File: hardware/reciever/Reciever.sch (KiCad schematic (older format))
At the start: 13 parts, among them J1 UART, J2 BTN, J3 OLED, P1 TC2030-CTX, SW1 RESET, U1 DS18B20, U2 BL654, U3 SHT30-DIS-B, U4 Coin Battery

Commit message: Add another schematic, add capacitor and rework 3v3 on laird
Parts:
- removed C1: 100nF, Capacitor_SMD:C_0603_1608Metric, symbol Device:C
- removed R4: 4,7k, Resistor_SMD:R_1206_3216Metric, symbol Device:R
- removed U1: DS18B20, Package_TO_SOT_THT:TO-92_Inline, symbol Sensor_Temperature:DS18B20
- removed U3: SHT30-DIS-B, SHT30-DIS-B:DFN250X250X100-9N, symbol SHT30-DIS-B:SHT30-DIS-B
- removed U4: Coin Battery, BS-3:BS3, symbol BS-3:BS-3
- added C? (x2): 100n, Capacitor_SMD:C_0805_2012Metric, symbol Device:C_Small
- added C? (x2): 10uF, symbol Device:CP_Small
- added C?: 22uF, symbol Device:CP_Small
- added D?: 1N5819HW-7-F, Diode_SMD:D_SOD-123, symbol Device:D_Schottky
- added J?: HEATER_CON, TerminalBlock_TE-Connectivity:TerminalBlock_TE_282834-2_1x02_P2.54mm_Horizontal, symbol Connector:Conn_01x02_Female
- added J?: PWR-9V, symbol Connector:Conn_01x02_Female
- added K?: RM50-xx21, Relay_THT:Relay_SPST_Finder_32.21-x300, symbol Relay:RM50-xx21
- added U?: DDC114EU, Package_TO_SOT_SMD:SOT-363_SC-70-6, symbol DDC114EU:DDC114EU
- added U?: AMS1117-3.3, Package_TO_SOT_SMD:SOT-223-3_TabPin2, symbol Regulator_Linear:AMS1117-3.3
- R1, R2: symbol Device:R -> Device:R_Small
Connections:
- net labels added: HEATER_PIN
- net labels removed: DS18B20
- wire segments 107 -> 128
- no-connect marks 44 -> 43
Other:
- moved on the sheet: J3

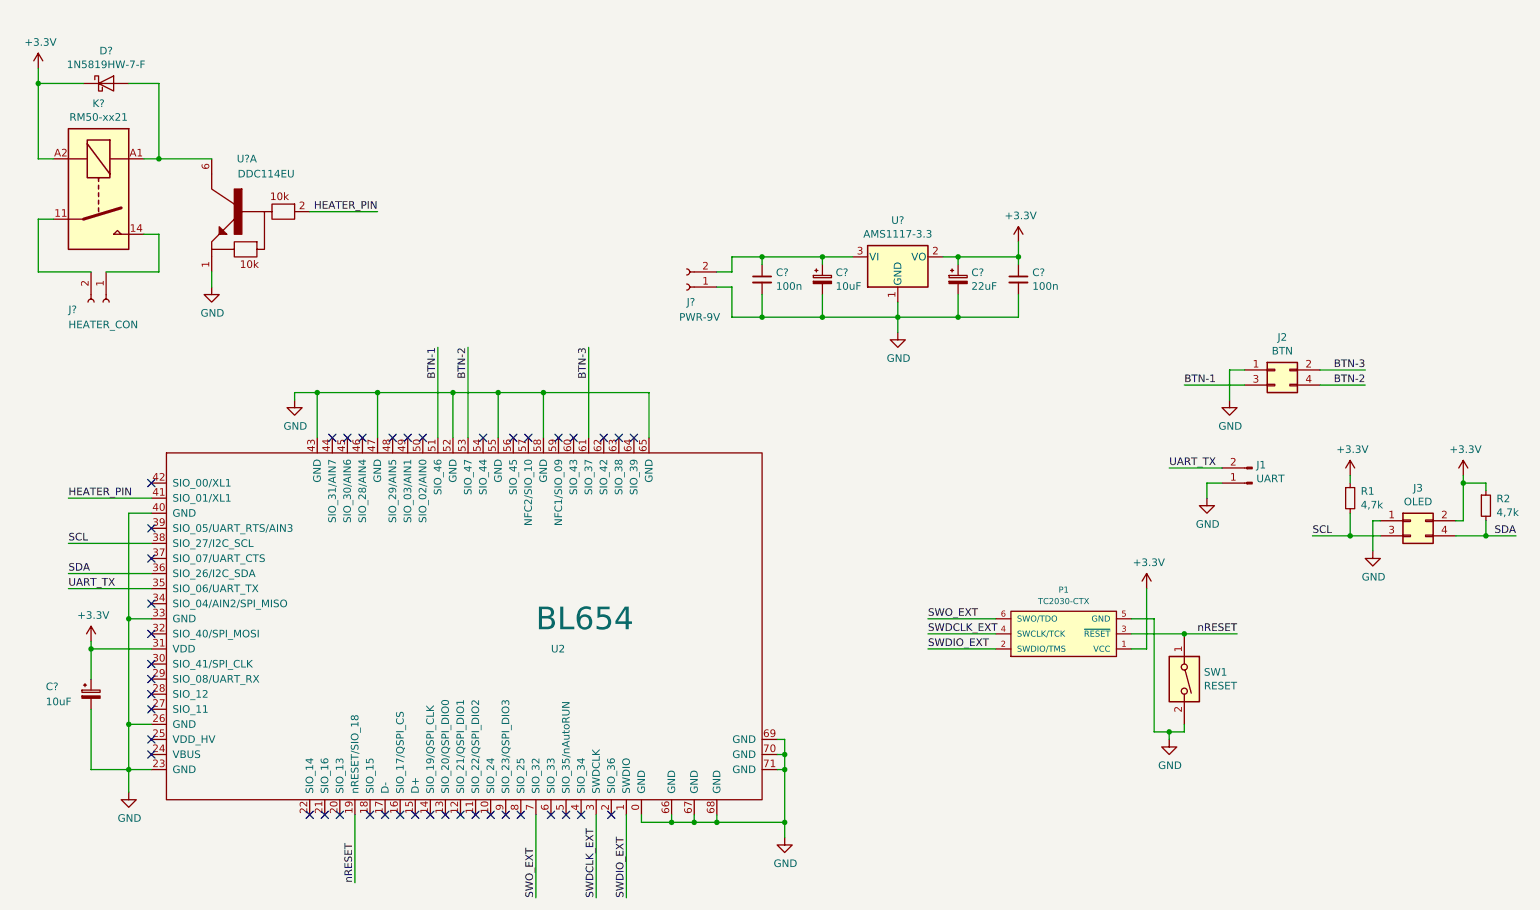
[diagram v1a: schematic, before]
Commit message: PCB layout fo reciever
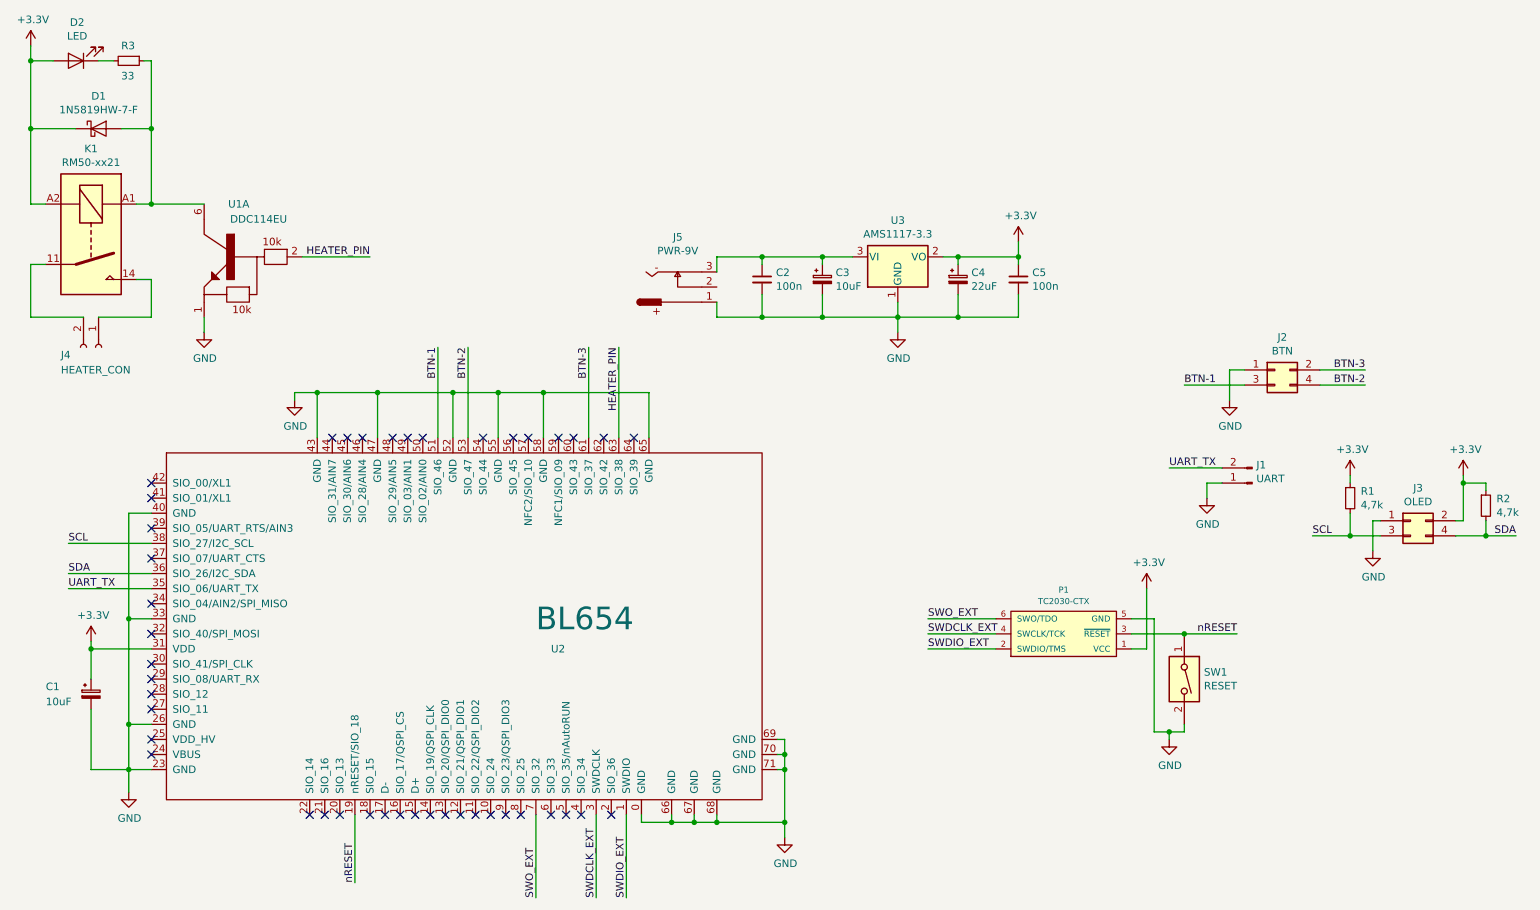
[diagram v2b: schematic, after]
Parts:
- removed J?: PWR-9V, symbol Connector:Conn_01x02_Female
- added D2: LED, Connector_PinHeader_2.54mm:PinHeader_1x02_P2.54mm_Vertical, symbol Device:LED
- added J5: PWR-9V, LUMBERG:1613-18, symbol Lumberg:1613-18
- added R3: 33, Resistor_SMD:R_1206_3216Metric, symbol Device:R_Small
- C1, C3, C4: renamed from C?; footprint (none) -> Capacitor_Tantalum_SMD:CP_EIA-3216-12_Kemet-S_Pad1.58x1.35mm_HandSolder
- gave numbers to parts that had none: 7
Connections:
- net +3V3: now also D2.2 (A)
- net GND: now also J5.1
- net HEATER_PIN: now also U2.63 (SIO_38); no longer U2.41 (SIO_01/XL1)
- net at D1.2 (A), K1.A1, U1.6: now also R3.1
- net at C2.1, C3.1, U3.3 (VI): now also J5.3
- new net: D2.1 (K), R3.2
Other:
- moved on the sheet: D1, J4, K1, U1A
